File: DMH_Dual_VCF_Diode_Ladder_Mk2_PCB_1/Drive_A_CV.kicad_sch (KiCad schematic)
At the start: 25 parts, among them J17 Conn_01x10_PinHeader, Q1 BC548, Q2 BC548, U1 TL074

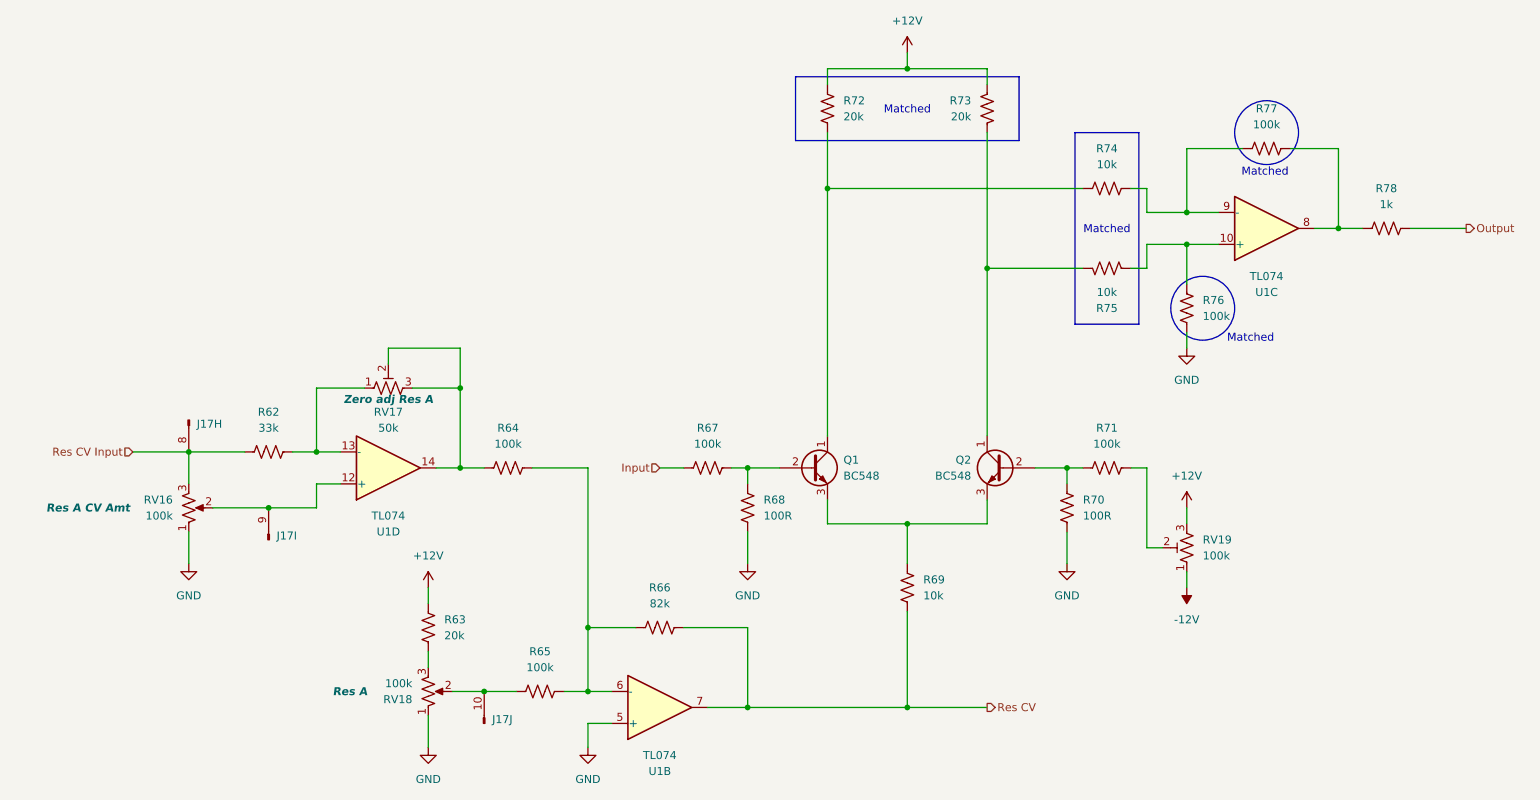
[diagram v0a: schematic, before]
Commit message: Created Drive CV circuits
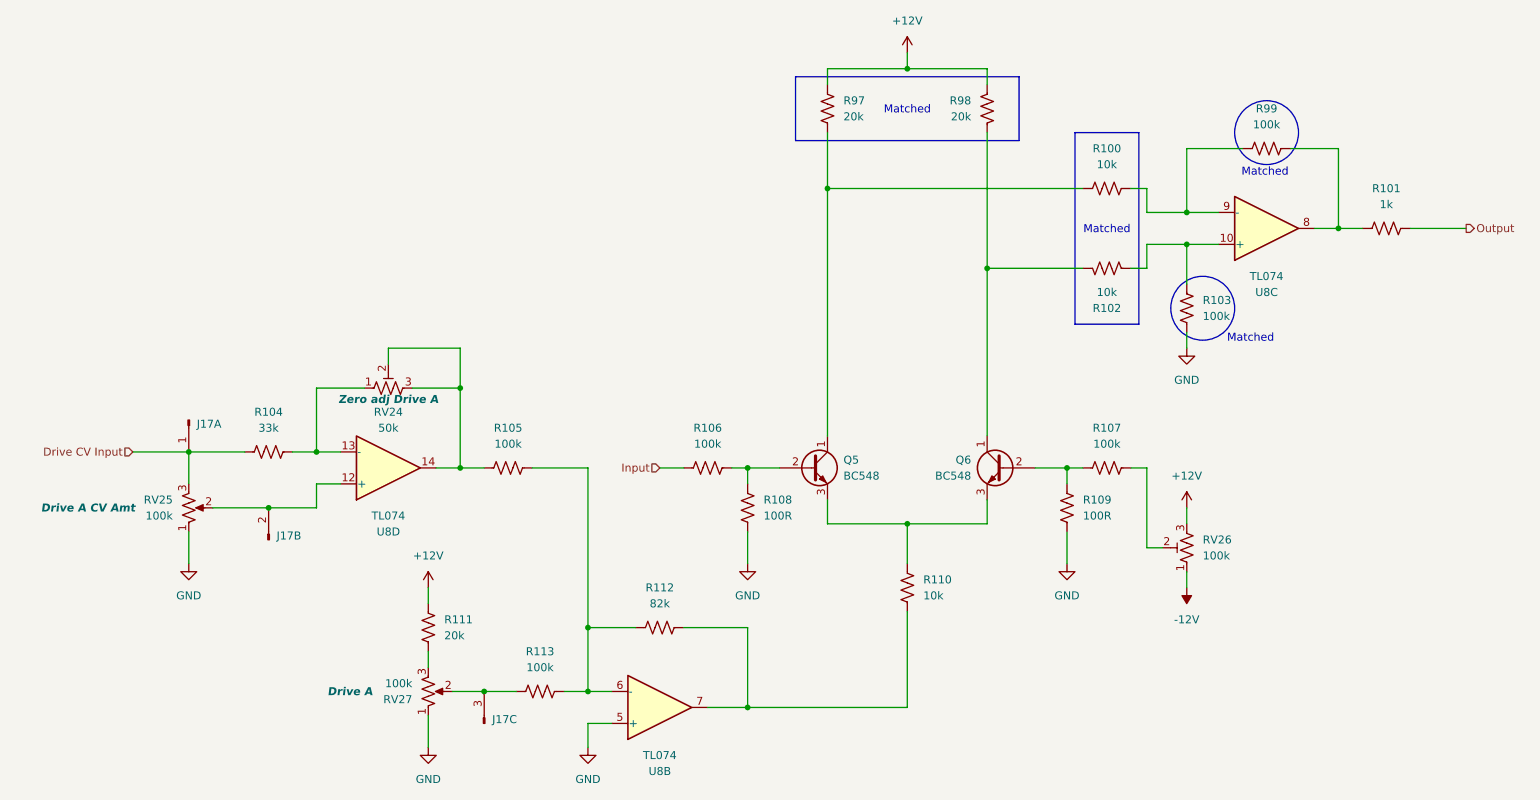
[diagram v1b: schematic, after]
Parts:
- RV24: renamed from RV17; Function Zero adj Res A -> Zero adj Drive A
- RV25: renamed from RV16; Function Res A CV Amt -> Drive A CV Amt
- RV27: renamed from RV18; Function Res A -> Drive A
- renumbered Q1 to Q5, Q2 to Q6, R74 to R100, R78 to R101, R75 to R102, R76 to R103, R62 to R104, R64 to R105, R67 to R106, R71 to R107, R68 to R108, R70 to R109, R69 to R110, R63 to R111, R66 to R112, R65 to R113, R72 to R97, R73 to R98, R77 to R99, RV19 to RV26, U1 to U8
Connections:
- net at R113.1, RV27.2: now also J17.3 (Pin_3); no longer J17.10 (Pin_10)
- net at RV25.2, U8.12 (+): now also J17.2 (Pin_2); no longer J17.9 (Pin_9)
- net Res CV: no longer names the net of R110.1, R112.2, U8.7
- net Res CV Input renamed Drive CV Input
- net Drive CV Input: now also J17.1 (Pin_1); no longer J17.8 (Pin_8)
